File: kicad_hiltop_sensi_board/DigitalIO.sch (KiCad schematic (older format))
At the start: 24 parts

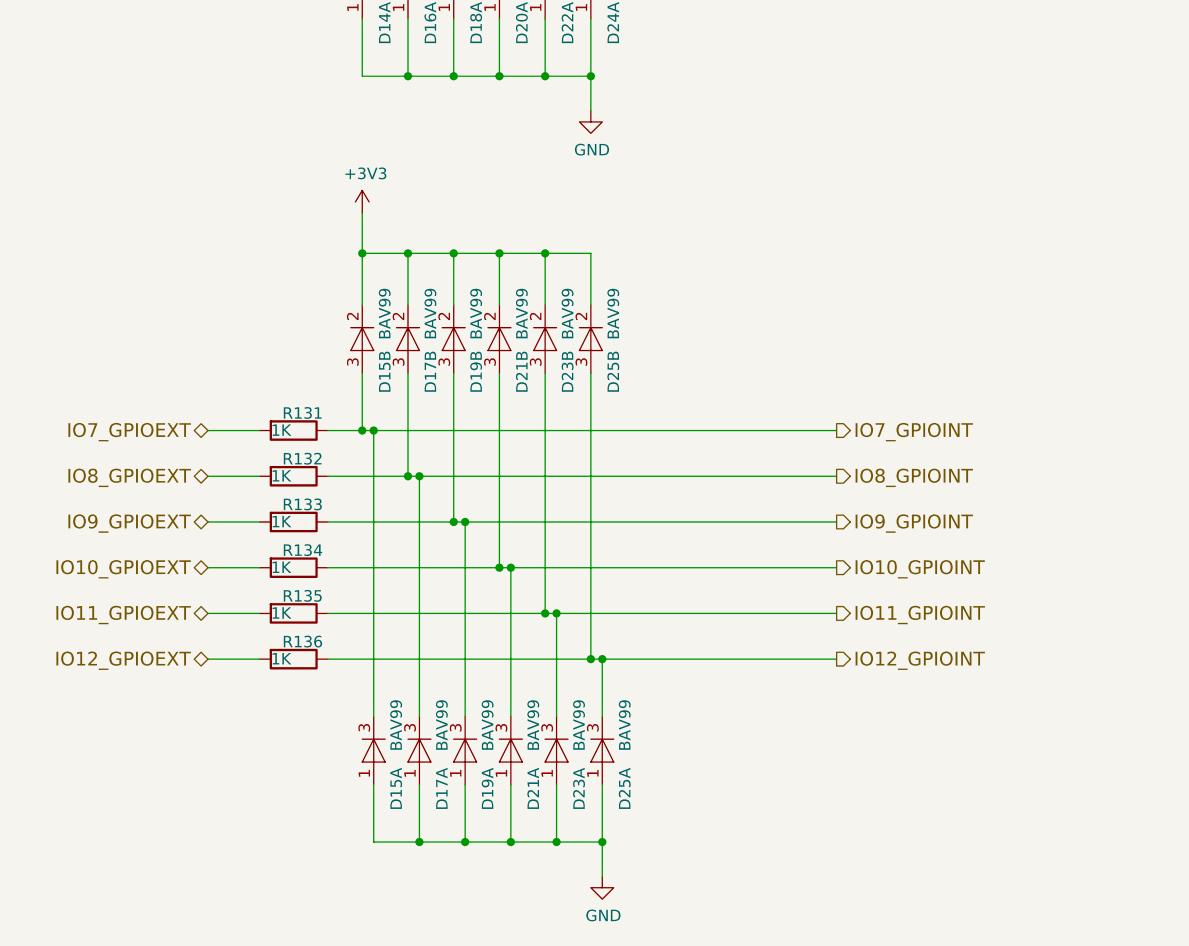
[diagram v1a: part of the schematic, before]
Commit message: Sensi board schematic updated from comments
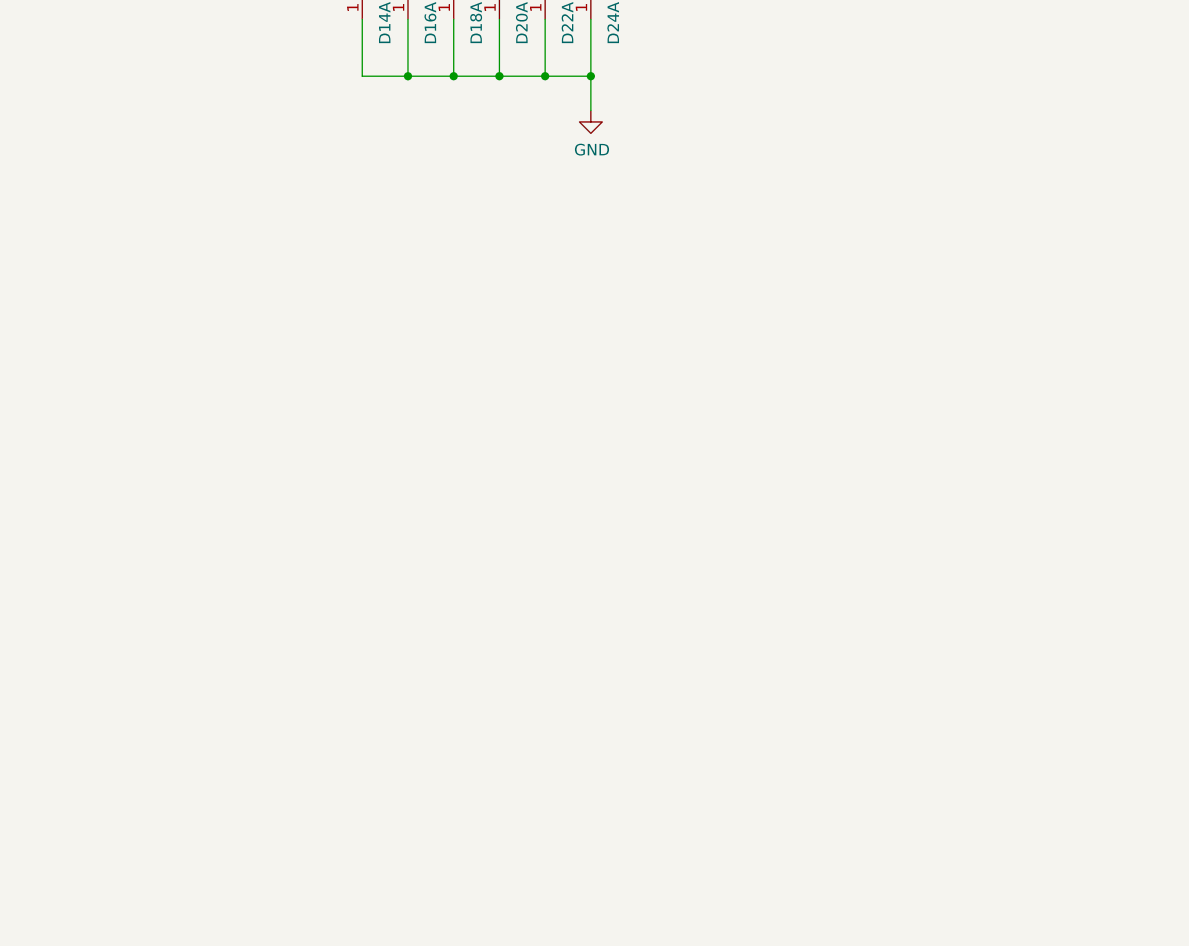
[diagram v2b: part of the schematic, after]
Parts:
- removed D15, D17, D19, D21, D23, D25: BAV99, Package_TO_SOT_SMD:SOT-23, symbol Diode:BAV99
- removed R131, R132, R133, R134, R135, R136: 1K, Resistor_SMD:R_0603_1608Metric, symbol Sensi_Board-rescue:R-device
